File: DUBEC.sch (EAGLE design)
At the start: 53 parts

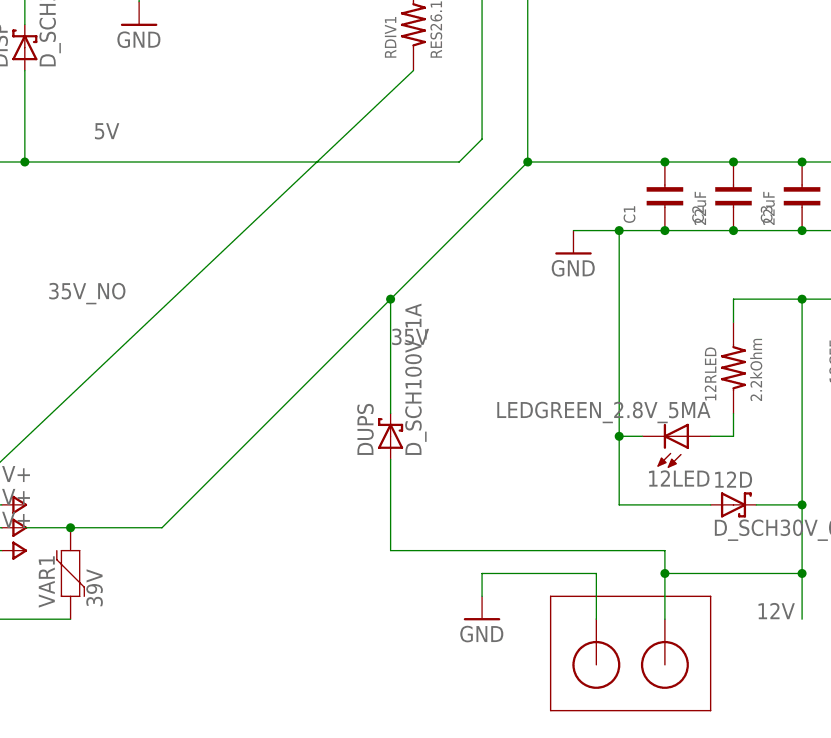
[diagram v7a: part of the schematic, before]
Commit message: Through-hole diode
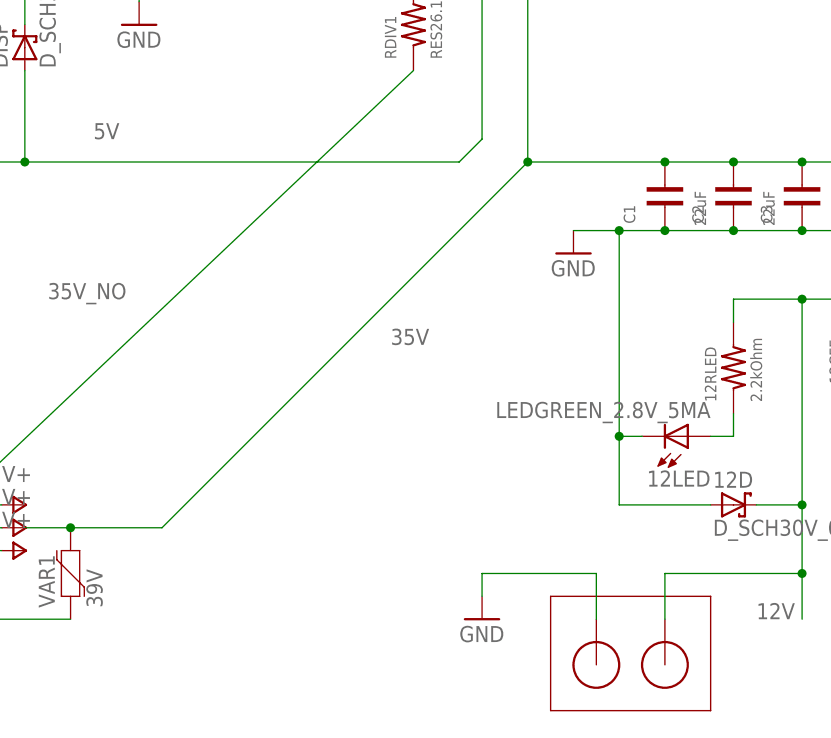
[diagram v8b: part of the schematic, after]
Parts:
- removed DUPS: D_SCH100V_1A, dubec:D_SCH100V_1A
- U$3, U$4: value H1 -> H10.65MM; device dubec:H1 -> dubec:H10.65MM
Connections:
- net 12V: no longer DUPS.A
- net 35V: no longer DUPS.C
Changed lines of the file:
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@@
 <part name="GND11" library="supply1" deviceset="GND" device=""/>
 <part name="C3" library="dubec" deviceset="CAP" device="22UF_35V" value="22uF"/>
-<part name="DUPS" library="dubec" deviceset="D_SCH" device="100V_1A" value="D_SCH100V_1A"/>
 <part name="GND12" library="supply1" deviceset="GND" device=""/>
 <part name="TP2" library="SparkFun-Passives" deviceset="TEST-POINT" device="3X5" value="TEST-POINT3X5"/>
-<part name="U$3" library="dubec" deviceset="H1" device=""/>
-<part name="U$4" library="dubec" deviceset="H1" device=""/>
+<part name="U$3" library="dubec" deviceset="H1" device="0.65MM"/>
+<part name="U$4" library="dubec" deviceset="H1" device="0.65MM"/>
 <part name="GND13" library="supply1" deviceset="GND" device=""/>
 </parts>
@@
 <instance part="GND11" gate="1" x="-22.86" y="50.8"/>
 <instance part="C3" gate="G$1" x="20.32" y="-12.7" rot="R90"/>
-<instance part="DUPS" gate="G$1" x="-25.4" y="-38.1" rot="R90"/>
 <instance part="GND12" gate="1" x="-73.66" y="-40.64"/>
 <instance part="TP2" gate="G$1" x="-27.94" y="30.48" rot="R270"/>
@@
 <wire x1="-66.04" y1="-48.26" x2="-60.96" y2="-48.26" width="0.1524" layer="91"/>
 <wire x1="-60.96" y1="-48.26" x2="-50.8" y2="-48.26" width="0.1524" layer="91"/>
-<wire x1="-50.8" y1="-48.26" x2="-25.4" y2="-22.86" width="0.1524" layer="91"/>
+<wire x1="-50.8" y1="-48.26" x2="-10.16" y2="-7.62" width="0.1524" layer="91"/>
 <junction x="-60.96" y="-48.26"/>
 <junction x="-10.16" y="-7.62"/>
 <pinref part="C3" gate="G$1" pin="2"/>
 <junction x="20.32" y="-7.62"/>
-<wire x1="-25.4" y1="-22.86" x2="-10.16" y2="-7.62" width="0.1524" layer="91"/>
 <wire x1="20.32" y1="-7.62" x2="60.96" y2="-7.62" width="0.1524" layer="91"/>
 <wire x1="60.96" y1="-7.62" x2="76.2" y2="-7.62" width="0.1524" layer="91"/>
@@
 <junction x="60.96" y="-7.62"/>
 <label x="-25.4" y="-27.94" size="1.778" layer="95"/>
-<pinref part="DUPS" gate="G$1" pin="C"/>
-<wire x1="-25.4" y1="-35.56" x2="-25.4" y2="-22.86" width="0.1524" layer="91"/>
-<junction x="-25.4" y="-22.86"/>
 </segment>
 <segment>
@@
 <wire x1="5.08" y1="-53.34" x2="20.32" y2="-53.34" width="0.1524" layer="91"/>
 <junction x="20.32" y="-53.34"/>
-<pinref part="DUPS" gate="G$1" pin="A"/>
-<wire x1="-25.4" y1="-40.64" x2="-25.4" y2="-50.8" width="0.1524" layer="91"/>
-<wire x1="-25.4" y1="-50.8" x2="5.08" y2="-50.8" width="0.1524" layer="91"/>
-<wire x1="5.08" y1="-50.8" x2="5.08" y2="-53.34" width="0.1524" layer="91"/>
-<junction x="5.08" y="-53.34"/>
-</segment>
-</net>
+</segment>
+</net>
